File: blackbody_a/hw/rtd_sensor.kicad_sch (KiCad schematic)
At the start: 6 parts, among them J1301 43650-0427, U1301 MAX31865AAP

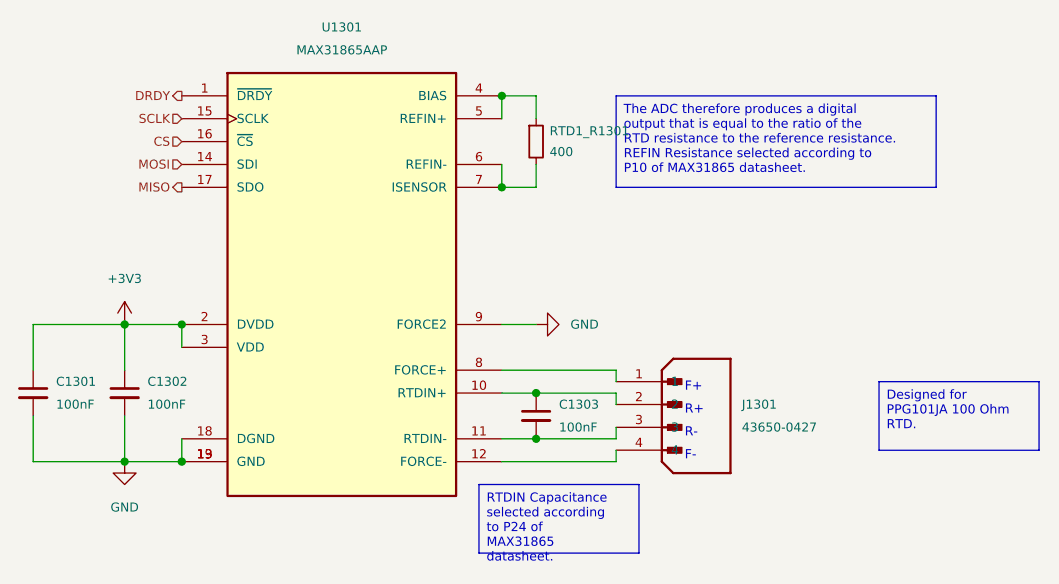
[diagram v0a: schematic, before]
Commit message: fixes for blackbody b before prod
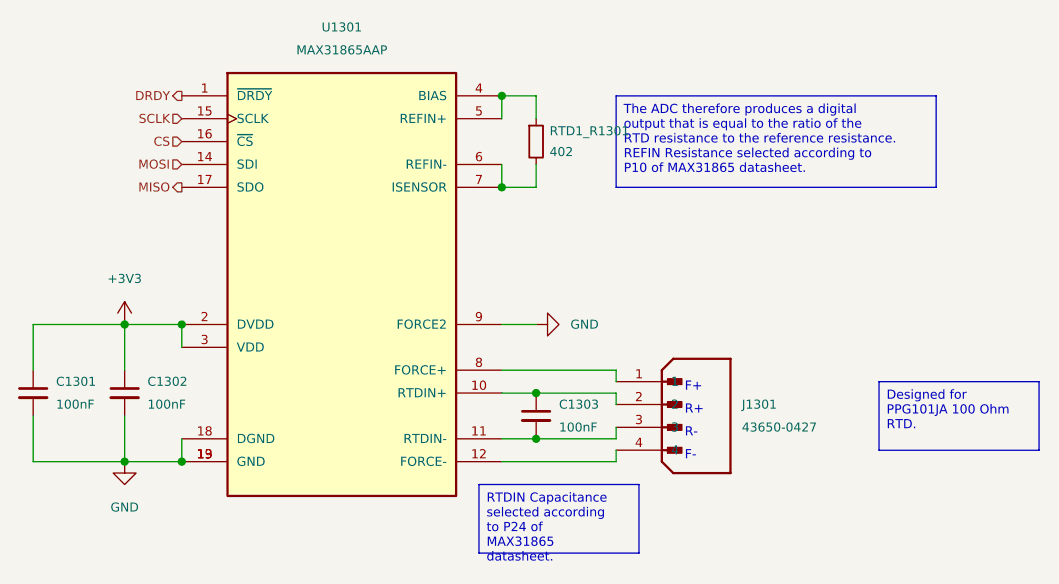
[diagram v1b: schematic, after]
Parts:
- RTD1_R1301: value 400 -> 402; Cost 0.0164 -> 0.13; Distributor JLCPCB -> Mouser; LCSC Part # C153298 -> (none); Manufacturer Ever Ohms Tech -> Yageo; Notes See Mouser for equivalent 0805 alternatives. -> Should be 400 ohms but good enough :(.; P/N TR0805B400RP0525Z -> RT0805DRE07402RL
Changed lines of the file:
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@@
       (effects (font (size 1 1)) (justify left))
     )
-    (property "Value" "400" (at 158.9786 76.073 0)
+    (property "Value" "402" (at 158.9786 76.073 0)
       (effects (font (size 1 1)) (justify left))
     )
@@
       (effects (font (size 1 1)) hide)
     )
-    (property "Datasheet" "https://jlcpcb.com/partdetail/Ever_OhmsTech-TR0805B400RP0525Z/C153298#:~:text=Datasheet-,Download,-Source" (at 157.48 74.93 0)
+    (property "Datasheet" "https://www.mouser.com/datasheet/2/447/PYu_RT_1_to_0_01_RoHS_L_12-3003070.pdf" (at 157.48 74.93 0)
       (effects (font (size 1 1)) hide)
     )
-    (property "Distributor" "JLCPCB" (at 157.48 74.93 0)
+    (property "Distributor" "Mouser" (at 157.48 74.93 0)
       (effects (font (size 1 1)) hide)
     )
-    (property "Manufacturer" "Ever Ohms Tech" (at 157.48 74.93 0)
+    (property "Manufacturer" "Yageo" (at 157.48 74.93 0)
       (effects (font (size 1 1)) hide)
     )
-    (property "P/N" "TR0805B400RP0525Z" (at 157.48 74.93 0)
+    (property "P/N" "RT0805DRE07402RL" (at 157.48 74.93 0)
       (effects (font (size 1 1)) hide)
     )
-    (property "LCSC Part #" "C153298" (at 157.48 74.93 0)
+    (property "LCSC Part #" "" (at 157.48 74.93 0)
       (effects (font (size 1 1)) hide)
     )
-    (property "Cost" "0.0164" (at 157.48 74.93 0)
+    (property "Cost" "0.13" (at 157.48 74.93 0)
       (effects (font (size 1 1)) hide)
     )
-    (property "Notes" "See Mouser for equivalent 0805 alternatives." (at 157.48 74.93 0)
+    (property "Notes" "Should be 400 ohms but good enough :(." (at 157.48 74.93 0)
       (effects (font (size 1 1)) hide)
     )
